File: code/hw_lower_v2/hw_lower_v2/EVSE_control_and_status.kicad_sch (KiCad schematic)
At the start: 16 parts, among them U3 DRV8220DRL, U4 TLV1805

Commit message: wip
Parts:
- D2: JLCPCB Part # C7473307 -> (none); LCSC (none) -> C7473307
- D3: JLCPCB Part # C908820 -> (none); LCSC (none) -> C908820
- U3: JLCPCB Part # C3681351 -> (none); LCSC (none) -> C3681351
- U4: JLCPCB Part # C2862164 -> (none); LCSC (none) -> C2862164
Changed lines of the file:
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@@
 			)
 		)
-		(property "JLCPCB Part #" "C3681351"
+		(property "LCSC" "C3681351"
 			(at 95.25 124.46 0)
 			(effects
@@
 			)
 		)
-		(property "JLCPCB Part #" ""
-			(at 74.93 152.4 0)
-			(effects
-				(font
-					(size 1.27 1.27)
-				)
-				(hide yes)
-			)
-		)
 		(pin "2"
 		)
@@
 			)
 		)
-		(property "JLCPCB Part #" ""
-			(at 87.63 55.88 0)
-			(effects
-				(font
-					(size 1.27 1.27)
-				)
-				(hide yes)
-			)
-		)
 		(pin "2"
 		)
@@
 		)
 		(property "Description" "Resistor"
-			(at 82.55 43.18 0)
-			(effects
-				(font
-					(size 1.27 1.27)
-				)
-				(hide yes)
-			)
-		)
-		(property "JLCPCB Part #" ""
 			(at 82.55 43.18 0)
 			(effects
@@
 			)
 		)
-		(property "JLCPCB Part #" "C908820"
+		(property "LCSC" "C908820"
 			(at 60.96 46.99 0)
 			(effects
@@
 			)
 		)
-		(property "JLCPCB Part #" "C2862164"
+		(property "LCSC" "C2862164"
 			(at 97.79 43.18 0)
 			(effects
@@
 		)
 		(property "Description" "Polarized capacitor"
-			(at 105.41 109.22 0)
-			(effects
-				(font
-					(size 1.27 1.27)
-				)
-				(hide yes)
-			)
-		)
-		(property "JLCPCB Part #" ""
 			(at 105.41 109.22 0)
 			(effects
@@
 			)
 		)
-		(property "JLCPCB Part #" "C7473307"
+		(property "LCSC" "C7473307"
 			(at 50.8 163.83 0)
 			(effects
@@
 			)
 		)
-		(property "JLCPCB Part #" ""
-			(at 121.92 53.34 0)
-			(effects
-				(font
-					(size 1.27 1.27)
-				)
-				(hide yes)
-			)
-		)
 		(pin "2"
 		)
@@
 		)
 		(property "Description" "Resistor"
-			(at 76.2 63.5 0)
-			(effects
-				(font
-					(size 1.27 1.27)
-				)
-				(hide yes)
-			)
-		)
-		(property "JLCPCB Part #" ""
 			(at 76.2 63.5 0)
 			(effects
@@
 			)
 		)
-		(property "JLCPCB Part #" ""
-			(at 121.92 63.5 0)
-			(effects
-				(font
-					(size 1.27 1.27)
-				)
-				(hide yes)
-			)
-		)
 		(pin "2"
 		)
@@
 			)
 		)
-		(property "JLCPCB Part #" ""
-			(at 101.6 54.61 0)
-			(effects
-				(font
-					(size 1.27 1.27)
-				)
-				(hide yes)
-			)
-		)
 		(pin "2"
 		)
@@
 			)
 		)
-		(property "JLCPCB Part #" ""
-			(at 101.6 25.4 0)
-			(effects
-				(font
-					(size 1.27 1.27)
-				)
-				(hide yes)
-			)
-		)
 		(pin "2"
 		)
@@
 			)
 		)
-		(property "JLCPCB Part #" ""
-			(at 74.93 86.36 0)
-			(effects
-				(font
-					(size 1.27 1.27)
-				)
-				(hide yes)
-			)
-		)
 		(pin "2"
 		)
@@
 			)
 		)
-		(property "JLCPCB Part #" ""
-			(at 76.2 55.88 0)
-			(effects
-				(font
-					(size 1.27 1.27)
-				)
-				(hide yes)
-			)
-		)
 		(pin "2"
 		)
@@
 			(at 114.3 109.22 0)
 			(effects
-				(font
-					(size 1.27 1.27)
-				)
-				(hide yes)
-			)
-		)
-		(property "JLCPCB Part #" ""
-			(at 114.3 109.22 0)
-			(effects

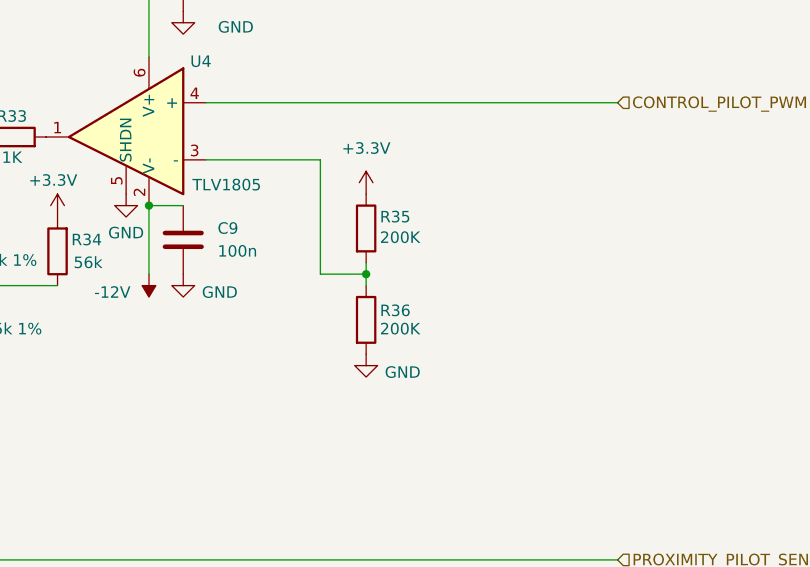
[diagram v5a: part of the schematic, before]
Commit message: finished schematic, started first pass of layout
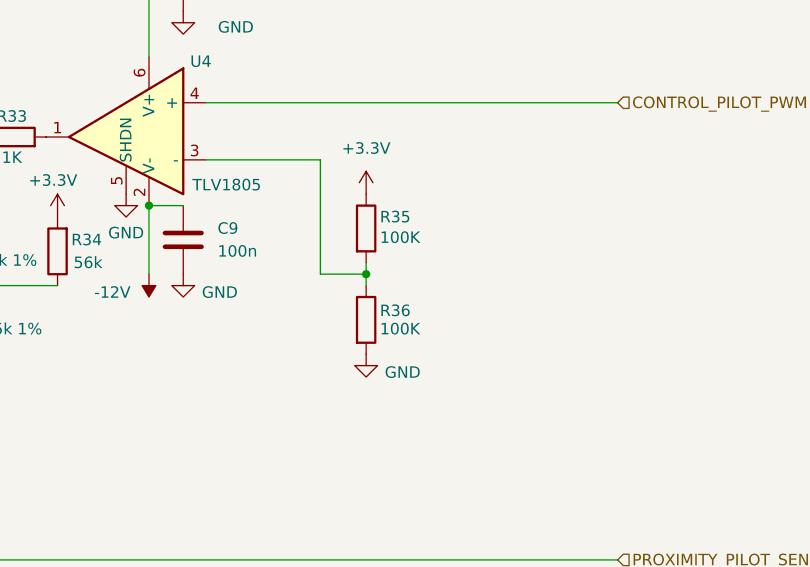
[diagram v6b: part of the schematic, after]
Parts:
- C10: value 10u -> 10u; footprint (none) -> Capacitor_SMD:CP_Elec_4x5.4; LCSC (none) -> C72485
- C11, C8, C9: LCSC (none) -> C38141
- R29, R33: LCSC (none) -> C21190
- R30: LCSC (none) -> C25804
- R31: LCSC (none) -> C2989567
- R32: LCSC (none) -> C861515
- R34: LCSC (none) -> C5250755
- R35, R36: value 200K -> 100K; LCSC (none) -> C25803
- U4: footprint Package_TO_SOT_SMD:SOT-23 -> JLCPCB:SOT-23-6_L2.9-W1.6-P0.95-LS2.8-BR
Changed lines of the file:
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@@
 		(on_board yes)
 		(dnp no)
-		(property "Reference" "#PWR047"
+		(property "Reference" "#PWR046"
 			(at 101.6 35.56 0)
 			(effects
@@
 			(project "hw_lower_v2"
 				(path "/c5175f1c-553a-46da-abbd-483c59ad8dfa/8ba574d6-efbf-49a1-9fad-b0d96c57b1a3"
-					(reference "#PWR047")
+					(reference "#PWR046")
 					(unit 1)
 				)
@@
 		(on_board yes)
 		(dnp no)
-		(property "Reference" "#PWR051"
+		(property "Reference" "#PWR050"
 			(at 121.92 73.66 0)
 			(effects
@@
 			(project "hw_lower_v2"
 				(path "/c5175f1c-553a-46da-abbd-483c59ad8dfa/8ba574d6-efbf-49a1-9fad-b0d96c57b1a3"
-					(reference "#PWR051")
+					(reference "#PWR050")
 					(unit 1)
 				)
@@
 		(dnp no)
 		(fields_autoplaced yes)
-		(property "Reference" "#PWR043"
+		(property "Reference" "#PWR042"
 			(at 95.25 105.41 0)
 			(effects
@@
 			(project ""
 				(path "/c5175f1c-553a-46da-abbd-483c59ad8dfa/8ba574d6-efbf-49a1-9fad-b0d96c57b1a3"
-					(reference "#PWR043")
+					(reference "#PWR042")
 					(unit 1)
 				)
@@
 			)
 		)
+		(property "LCSC" "C25804"
+			(at 74.93 152.4 0)
+			(effects
+				(font
+					(size 1.27 1.27)
+				)
+				(hide yes)
+			)
+		)
 		(pin "2"
 		)
@@
 		(dnp no)
 		(fields_autoplaced yes)
-		(property "Reference" "#PWR049"
+		(property "Reference" "#PWR048"
 			(at 110.49 119.38 0)
 			(effects
@@
 			(project "hw_lower_v2"
 				(path "/c5175f1c-553a-46da-abbd-483c59ad8dfa/8ba574d6-efbf-49a1-9fad-b0d96c57b1a3"
-					(reference "#PWR049")
+					(reference "#PWR048")
 					(unit 1)
 				)
@@
 			)
 		)
+		(property "LCSC" "C5250755"
+			(at 87.63 55.88 0)
+			(effects
+				(font
+					(size 1.27 1.27)
+				)
+				(hide yes)
+			)
+		)
 		(pin "2"
 		)
@@
 		(on_board yes)
 		(dnp no)
-		(property "Reference" "#PWR046"
+		(property "Reference" "#PWR045"
 			(at 97.79 54.61 0)
 			(effects
@@
 			(project ""
 				(path "/c5175f1c-553a-46da-abbd-483c59ad8dfa/8ba574d6-efbf-49a1-9fad-b0d96c57b1a3"
-					(reference "#PWR046")
+					(reference "#PWR045")
 					(unit 1)
 				)
@@
 		)
 		(property "Description" "Resistor"
+			(at 82.55 43.18 0)
+			(effects
+				(font
+					(size 1.27 1.27)
+				)
+				(hide yes)
+			)
+		)
+		(property "LCSC" "C21190"
 			(at 82.55 43.18 0)
 			(effects
@@
 		(dnp no)
 		(fields_autoplaced yes)
-		(property "Reference" "#PWR050"
+		(property "Reference" "#PWR049"
 			(at 121.92 53.34 0)
 			(effects
@@
 			(project "hw_lower_v2"
 				(path "/c5175f1c-553a-46da-abbd-483c59ad8dfa/8ba574d6-efbf-49a1-9fad-b0d96c57b1a3"
-					(reference "#PWR050")
+					(reference "#PWR049")
 					(unit 1)
 				)
@@
 			)
 		)
-		(property "Footprint" "Package_TO_SOT_SMD:SOT-23"
+		(property "Footprint" "JLCPCB:SOT-23-6_L2.9-W1.6-P0.95-LS2.8-BR"
 			(at 99.06 43.18 0)
 			(effects
@@
 		(on_board yes)
 		(dnp no)
-		(property "Reference" "#PWR042"
+		(property "Reference" "#PWR041"
 			(at 95.25 55.88 0)
 			(effects
@@
 			(project "hw_lower_v2"
 				(path "/c5175f1c-553a-46da-abbd-483c59ad8dfa/8ba574d6-efbf-49a1-9fad-b0d96c57b1a3"
-					(reference "#PWR042")
+					(reference "#PWR041")
 					(unit 1)
 				)
@@
 		(on_board yes)
 		(dnp no)
-		(property "Reference" "#PWR040"
+		(property "Reference" "#PWR039"
 			(at 76.2 73.66 0)
 			(effects
@@
 			(project "hw_lower_v2"
 				(path "/c5175f1c-553a-46da-abbd-483c59ad8dfa/8ba574d6-efbf-49a1-9fad-b0d96c57b1a3"
-					(reference "#PWR040")
+					(reference "#PWR039")
 					(unit 1)
 				)
@@
 		(on_board yes)
 		(dnp no)
-		(property "Reference" "#PWR048"
+		(property "Reference" "#PWR047"
 			(at 101.6 64.77 0)
 			(effects
@@
 			(project "hw_lower_v2"
 				(path "/c5175f1c-553a-46da-abbd-483c59ad8dfa/8ba574d6-efbf-49a1-9fad-b0d96c57b1a3"
-					(reference "#PWR048")
+					(reference "#PWR047")
 					(unit 1)
 				)
@@
 			)
 		)
-		(property "Value" " 10u"
+		(property "Value" "10u"
 			(at 105.156 111.76 0)
 			(effects
@@
 			)
 		)
-		(property "Footprint" ""
+		(property "Footprint" "Capacitor_SMD:CP_Elec_4x5.4"
 			(at 106.3752 113.03 0)
 			(effects
@@
 			)
 		)
+		(property "LCSC" "C72485"
+			(at 105.41 109.22 0)
+			(effects
+				(font
+					(size 1.27 1.27)
+				)
+				(hide yes)
+			)
+		)
 		(pin "1"
 		)
@@
 		(dnp no)
 		(fields_autoplaced yes)
-		(property "Reference" "#PWR039"
+		(property "Reference" "#PWR038"
 			(at 74.93 152.4 0)
 			(effects
@@
 			(project "hw_lower_v2"
 				(path "/c5175f1c-553a-46da-abbd-483c59ad8dfa/8ba574d6-efbf-49a1-9fad-b0d96c57b1a3"
-					(reference "#PWR039")
+					(reference "#PWR038")
 					(unit 1)
 				)
@@
 		(dnp no)
 		(fields_autoplaced yes)
-		(property "Reference" "#PWR045"
+		(property "Reference" "#PWR044"
 			(at 97.79 24.13 0)
 			(effects
@@
 			(project ""
 				(path "/c5175f1c-553a-46da-abbd-483c59ad8dfa/8ba574d6-efbf-49a1-9fad-b0d96c57b1a3"
-					(reference "#PWR045")
+					(reference "#PWR044")
 					(unit 1)
 				)
@@
 		(dnp no)
 		(fields_autoplaced yes)
-		(property "Reference" "#PWR044"
+		(property "Reference" "#PWR043"
 			(at 95.25 143.51 0)
 			(effects
@@
 			(project ""
 				(path "/c5175f1c-553a-46da-abbd-483c59ad8dfa/8ba574d6-efbf-49a1-9fad-b0d96c57b1a3"
-					(reference "#PWR044")
+					(reference "#PWR043")
 					(unit 1)
 				)
@@
 			)
 		)
-		(property "Value" "200K"
+		(property "Value" "100K"
 			(at 123.444 54.356 0)
 			(effects
@@
 			)
 		)
+		(property "LCSC" "C25803"
+			(at 121.92 53.34 0)
+			(effects
+				(font
+					(size 1.27 1.27)
+				)
+				(hide yes)
+			)
+		)
 		(pin "2"
 		)
@@
 			)
 		)
+		(property "LCSC" "C861515"
+			(at 76.2 63.5 0)
+			(effects
+				(font
+					(size 1.27 1.27)
+				)
+				(hide yes)
+			)
+		)
 		(pin "2"
 		)
@@
 		(dnp no)
 		(fields_autoplaced yes)
-		(property "Reference" "#PWR038"
+		(property "Reference" "#PWR037"
 			(at 74.93 86.36 0)
 			(effects
@@
 			(project ""
 				(path "/c5175f1c-553a-46da-abbd-483c59ad8dfa/8ba574d6-efbf-49a1-9fad-b0d96c57b1a3"
-					(reference "#PWR038")
+					(reference "#PWR037")
 					(unit 1)
 				)
@@
 			)
 		)
-		(property "Value" "200K"
+		(property "Value" "100K"
 			(at 123.444 64.516 0)
 			(effects
@@
 			)
 		)
+		(property "LCSC" "C25803"
+			(at 121.92 63.5 0)
+			(effects
+				(font
+					(size 1.27 1.27)
+				)
+				(hide yes)
+			)
+		)
 		(pin "2"
 		)
@@
 		(on_board yes)
 		(dnp no)
-		(property "Reference" "#PWR041"
+		(property "Reference" "#PWR040"
 			(at 87.63 55.88 0)
 			(effects
@@
 			(project "hw_lower_v2"
 				(path "/c5175f1c-553a-46da-abbd-483c59ad8dfa/8ba574d6-efbf-49a1-9fad-b0d96c57b1a3"
-					(reference "#PWR041")
+					(reference "#PWR040")
 					(unit 1)
 				)
@@
 		(on_board yes)
 		(dnp no)
-		(property "Reference" "#PWR037"
+		(property "Reference" "#PWR036"
 			(at 60.96 57.15 0)
 			(effects
@@
 			(project "hw_lower_v2"
 				(path "/c5175f1c-553a-46da-abbd-483c59ad8dfa/8ba574d6-efbf-49a1-9fad-b0d96c57b1a3"
-					(reference "#PWR037")
+					(reference "#PWR036")
 					(unit 1)
 				)
@@
 			)
 		)
+		(property "LCSC" "C38141"
+			(at 101.6 54.61 0)
+			(effects
+				(font
+					(size 1.27 1.27)
+				)
+				(hide yes)
+			)
+		)
 		(pin "2"
 		)
@@
 			)
 		)
+		(property "LCSC" "C38141"
+			(at 101.6 25.4 0)
+			(effects
+				(font
+					(size 1.27 1.27)
+				)
+				(hide yes)
+			)
+		)
 		(pin "2"
 		)
@@
 			)
 		)
+		(property "LCSC" "C21190"
+			(at 74.93 86.36 0)
+			(effects
+				(font
+					(size 1.27 1.27)
+				)
+				(hide yes)
+			)
+		)
 		(pin "2"
 		)
@@
 			)
 		)
+		(property "LCSC" "C2989567"
+			(at 76.2 55.88 0)
+			(effects
+				(font
+					(size 1.27 1.27)
+				)
+				(hide yes)
+			)
+		)
 		(pin "2"
 		)
@@
 			)
 		)
+		(property "LCSC" "C38141"
+			(at 114.3 109.22 0)
+			(effects
+				(font
+					(size 1.27 1.27)
+				)
+				(hide yes)
+			)
+		)
 		(pin "2"
 		)
@@
 		(dnp no)
 		(fields_autoplaced yes)
-		(property "Reference" "#PWR036"
+		(property "Reference" "#PWR035"
 			(at 50.8 182.88 0)
 			(effects
@@
 			(project "hw_lower_v2"
 				(path "/c5175f1c-553a-46da-abbd-483c59ad8dfa/8ba574d6-efbf-49a1-9fad-b0d96c57b1a3"
-					(reference "#PWR036")
-					(unit 1)
-				)
+					(reference "#PWR035")
+					(unit 1)
+				)

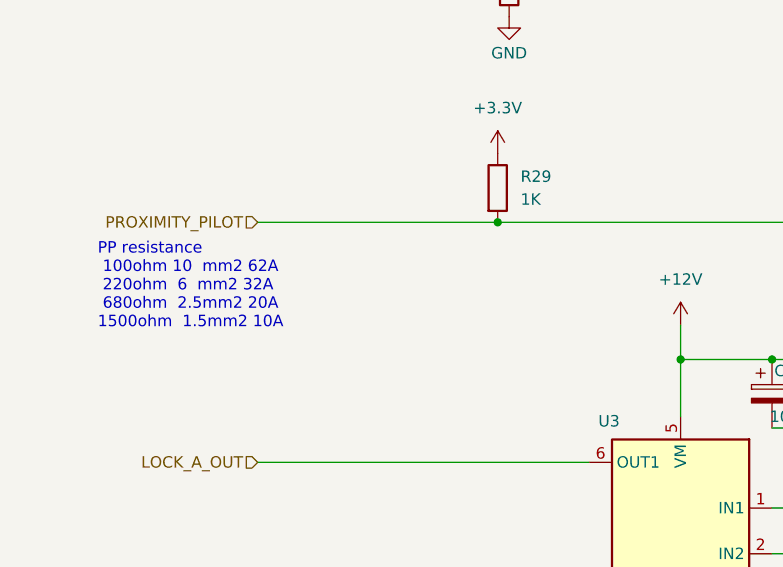
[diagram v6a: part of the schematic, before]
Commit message: Preliminary pcb component placement done
PCB size currently is around 100mm X 100mm with the mezanine board being ~40mm x 100mm
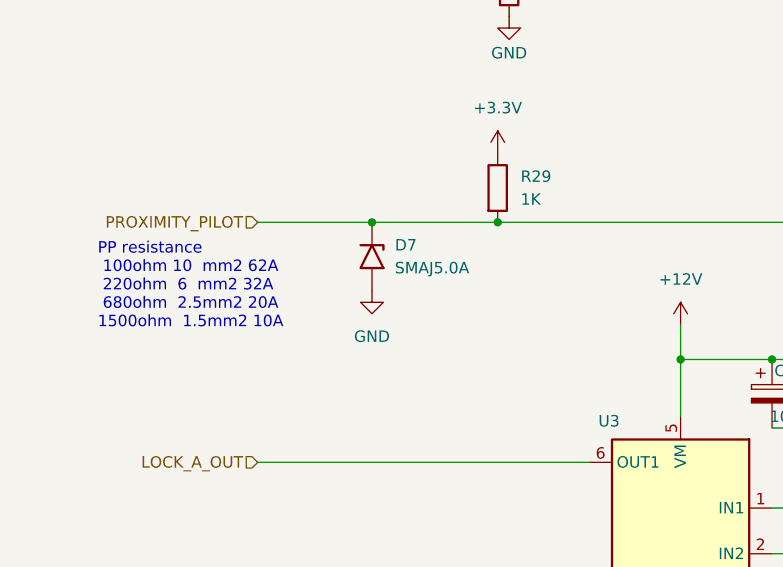
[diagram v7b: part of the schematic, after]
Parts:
- added D7: SMAJ5.0A, Diode_SMD:D_SMA, symbol Diode:SMAJ5.0A
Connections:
- net GND: now also D7.2 (A2)
- net PROXIMITY_PILOT: now also D7.1 (A1)
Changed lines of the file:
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@@
+	)
+	(junction
+		(at 60.96 90.17)
+		(diameter 0)
+		(color 0 0 0 0)
 	)
 	(junction
@@
 	(wire
 		(pts
+			(xy 60.96 90.17) (xy 74.93 90.17)
+		)
+		(stroke
+			(width 0)
+			(type default)
+		)
+	)
+	(wire
+		(pts
 			(xy 87.63 59.69) (xy 76.2 59.69)
 		)
@@
 	(wire
 		(pts
-			(xy 48.26 90.17) (xy 74.93 90.17)
+			(xy 48.26 90.17) (xy 60.96 90.17)
 		)
 		(stroke
@@
 	)
 	(symbol
+		(lib_id "power:GND")
+		(at 60.96 97.79 0)
+		(unit 1)
+		(exclude_from_sim no)
+		(in_bom yes)
+		(on_board yes)
+		(dnp no)
+		(fields_autoplaced yes)
+		(property "Reference" "#PWR063"
+			(at 60.96 104.14 0)
+			(effects
+				(font
+					(size 1.27 1.27)
+				)
+				(hide yes)
+			)
+		)
+		(property "Value" "GND"
+			(at 60.96 102.87 0)
+			(effects
+				(font
+					(size 1.27 1.27)
+				)
+			)
+		)
+		(property "Footprint" ""
+			(at 60.96 97.79 0)
+			(effects
+				(font
+					(size 1.27 1.27)
+				)
+				(hide yes)
+			)
+		)
+		(property "Datasheet" ""
+			(at 60.96 97.79 0)
+			(effects
+				(font
+					(size 1.27 1.27)
+				)
+				(hide yes)
+			)
+		)
+		(property "Description" "Power symbol creates a global label with name \"GND\" , ground"
+			(at 60.96 97.79 0)
+			(effects
+				(font
+					(size 1.27 1.27)
+				)
+				(hide yes)
+			)
+		)
+		(pin "1"
+		)
+		(instances
+			(project "hw_lower_v2"
+				(path "/c5175f1c-553a-46da-abbd-483c59ad8dfa/8ba574d6-efbf-49a1-9fad-b0d96c57b1a3"
+					(reference "#PWR063")
+					(unit 1)
+				)
+			)
+		)
+	)
+	(symbol
 		(lib_id "Device:R")
 		(at 76.2 63.5 180)
@@
 					(unit 1)
 				)
+			)
+		)
+	)
+	(symbol
+		(lib_id "Diode:SMAJ5.0A")
+		(at 60.96 93.98 270)
+		(unit 1)
+		(exclude_from_sim no)
+		(in_bom yes)
+		(on_board yes)
+		(dnp no)
+		(fields_autoplaced yes)
+		(property "Reference" "D7"
+			(at 63.5 92.7099 90)
+			(effects
+				(font
+					(size 1.27 1.27)
+				)
+				(justify left)
+			)
+		)
+		(property "Value" "SMAJ5.0A"
+			(at 63.5 95.2499 90)
+			(effects
+				(font
+					(size 1.27 1.27)
+				)
+				(justify left)
+			)
+		)
+		(property "Footprint" "Diode_SMD:D_SMA"
+			(at 55.88 93.98 0)
+			(effects
+				(font
+					(size 1.27 1.27)
+				)
+				(hide yes)
+			)
+		)
+		(property "Datasheet" "https://www.littelfuse.com/media?resourcetype=datasheets&itemid=75e32973-b177-4ee3-a0ff-cedaf1abdb93&filename=smaj-datasheet"
+			(at 60.96 92.71 0)
+			(effects
+				(font
+					(size 1.27 1.27)
+				)
+				(hide yes)
+			)
+		)
+		(property "Description" "400W unidirectional Transient Voltage Suppressor, 5.0Vr, SMA(DO-214AC)"
+			(at 60.96 93.98 0)
+			(effects
+				(font
+					(size 1.27 1.27)
+				)
+				(hide yes)
+			)
+		)
+		(property "LCSC" "C7473307"
+			(at 60.96 93.98 0)
+			(effects
+				(font
+					(size 1.27 1.27)
+				)
+				(hide yes)
+			)
+		)
+		(pin "1"
+		)
+		(pin "2"
+		)
+		(instances
+			(project "hw_lower_v2"
+				(path "/c5175f1c-553a-46da-abbd-483c59ad8dfa/8ba574d6-efbf-49a1-9fad-b0d96c57b1a3"
+					(reference "D7")
+					(unit 1)
+				)

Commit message: have one project part library
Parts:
- U4: footprint JLCPCB:SOT-23-6_L2.9-W1.6-P0.95-LS2.8-BR -> multi_new:SOT-23-6_L2.9-W1.6-P0.95-LS2.8-BR
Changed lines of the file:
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@@
+			)
+		)
+		(property "Name" ""
+			(at 95.25 124.46 0)
+			(effects
+				(font
+					(size 1.27 1.27)
+				)
+				(hide yes)
 			)
 		)
@@
 			)
 		)
+		(property "Name" ""
+			(at 74.93 152.4 0)
+			(effects
+				(font
+					(size 1.27 1.27)
+				)
+				(hide yes)
+			)
+		)
 		(pin "2"
 		)
@@
 			)
 		)
+		(property "Name" ""
+			(at 87.63 55.88 0)
+			(effects
+				(font
+					(size 1.27 1.27)
+				)
+				(hide yes)
+			)
+		)
 		(pin "2"
 		)
@@
 		)
 		(property "LCSC" "C21190"
+			(at 82.55 43.18 0)
+			(effects
+				(font
+					(size 1.27 1.27)
+				)
+				(hide yes)
+			)
+		)
+		(property "Name" ""
 			(at 82.55 43.18 0)
 			(effects
@@
 			)
 		)
+		(property "Name" ""
+			(at 60.96 46.99 0)
+			(effects
+				(font
+					(size 1.27 1.27)
+				)
+				(hide yes)
+			)
+		)
 		(pin "2"
 		)
@@
 			)
 		)
-		(property "Footprint" "JLCPCB:SOT-23-6_L2.9-W1.6-P0.95-LS2.8-BR"
+		(property "Footprint" "multi_new:SOT-23-6_L2.9-W1.6-P0.95-LS2.8-BR"
 			(at 99.06 43.18 0)
 			(effects
@@
 			)
 		)
+		(property "Name" ""
+			(at 97.79 43.18 0)
+			(effects
+				(font
+					(size 1.27 1.27)
+				)
+				(hide yes)
+			)
+		)
 		(pin "1"
 		)
@@
 		)
 		(property "LCSC" "C72485"
+			(at 105.41 109.22 0)
+			(effects
+				(font
+					(size 1.27 1.27)
+				)
+				(hide yes)
+			)
+		)
+		(property "Name" ""
 			(at 105.41 109.22 0)
 			(effects
@@
 			)
 		)
+		(property "Name" ""
+			(at 50.8 163.83 0)
+			(effects
+				(font
+					(size 1.27 1.27)
+				)
+				(hide yes)
+			)
+		)
 		(pin "1"
 		)
@@
 		)
 		(property "LCSC" "C25803"
+			(at 121.92 53.34 0)
+			(effects
+				(font
+					(size 1.27 1.27)
+				)
+				(hide yes)
+			)
+		)
+		(property "Name" ""
 			(at 121.92 53.34 0)
 			(effects
@@
 			)
 		)
+		(property "Name" ""
+			(at 76.2 63.5 0)
+			(effects
+				(font
+					(size 1.27 1.27)
+				)
+				(hide yes)
+			)
+		)
 		(pin "2"
 		)
@@
 			)
 		)
+		(property "Name" ""
+			(at 121.92 63.5 0)
+			(effects
+				(font
+					(size 1.27 1.27)
+				)
+				(hide yes)
+			)
+		)
 		(pin "2"
 		)
@@
 			)
 		)
+		(property "Name" ""
+			(at 101.6 54.61 0)
+			(effects
+				(font
+					(size 1.27 1.27)
+				)
+				(hide yes)
+			)
+		)
 		(pin "2"
 		)
@@
 			)
 		)
+		(property "Name" ""
+			(at 101.6 25.4 0)
+			(effects
+				(font
+					(size 1.27 1.27)
+				)
+				(hide yes)
+			)
+		)
 		(pin "2"
 		)
@@
 			)
 		)
+		(property "Name" ""
+			(at 74.93 86.36 0)
+			(effects
+				(font
+					(size 1.27 1.27)
+				)
+				(hide yes)
+			)
+		)
 		(pin "2"
 		)
@@
 			)
 		)
+		(property "Name" ""
+			(at 60.96 93.98 0)
+			(effects
+				(font
+					(size 1.27 1.27)
+				)
+				(hide yes)
+			)
+		)
 		(pin "1"
 		)
@@
 			)
 		)
+		(property "Name" ""
+			(at 76.2 55.88 0)
+			(effects
+				(font
+					(size 1.27 1.27)
+				)
+				(hide yes)
+			)
+		)
 		(pin "2"
 		)
@@
 			(at 114.3 109.22 0)
 			(effects
+				(font
+					(size 1.27 1.27)
+				)
+				(hide yes)
+			)
+		)
+		(property "Name" ""
+			(at 114.3 109.22 0)
+			(effects
